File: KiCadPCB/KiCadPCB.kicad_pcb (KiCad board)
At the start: 2 copper layers, 152.4 x 50.2 mm, 29 parts, among them SW1 M1, SW10 M10, SW11 M11, SW12 M12, SW13 M13, SW14 ENCODER, SW2 M2, SW3 M3, SW4 M4, SW5 M5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

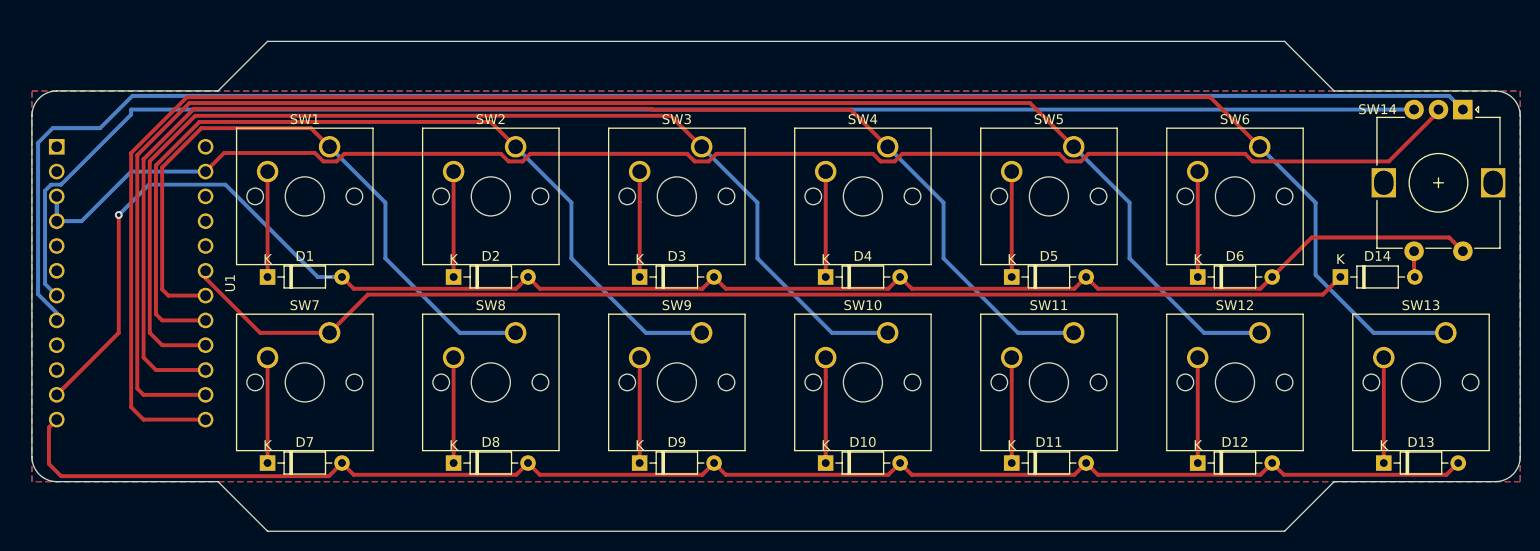
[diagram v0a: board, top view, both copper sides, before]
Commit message: Added gerber files and updated the PCB files.
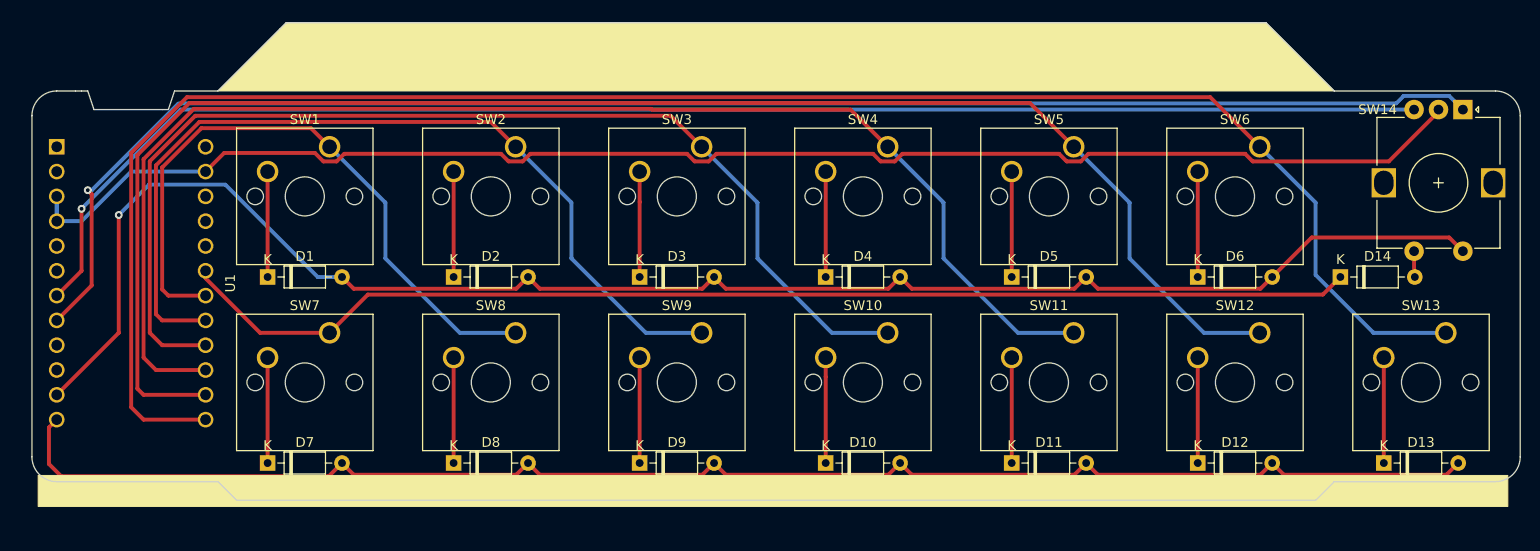
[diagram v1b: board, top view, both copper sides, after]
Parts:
- added H1: MountingHole, MountingHole:MountingHole_3.2mm_M3, F.Cu at (105.4, 27.9)
- added H2: MountingHole, MountingHole:MountingHole_3.2mm_M3, F.Cu at (202.6, 27.9)
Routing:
- net Net-(SW14-PadA): track 167.4 -> 160.4 mm, vias 0 -> 1
- net Net-(SW14-PadB): track 155.2 -> 150.6 mm, vias 0 -> 1
- removed copper zone on B.Cu, net GND
- removed copper zone on F.Cu, net GND
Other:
- board size 152.4 x 50.2 mm -> 152.4 x 48.9 mm

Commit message: Updated the PCB file as the last prototype revision
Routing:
- net Net-(SW14-PadB): track 150.6 -> 152.2 mm
- net Net-(SW14-PadA): track 160.4 -> 159.2 mm
- added copper zone on B.Cu, net (none)
- added copper zone on F.Cu, net GND
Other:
- board text added: "JLCJLCJLCJLC"
- board text added: "Le Fishe au Macropad"
